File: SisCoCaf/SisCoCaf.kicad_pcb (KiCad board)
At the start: 2 copper layers, 20 parts, among them IC1 LPC111X_102, J1 Conn_01x02_Female, J2 Conn_01x02_Female, J3 Conn_01x03_Male, J4 Conn_01x03_Male, J5 Conn_01x01_Male, Q1 BC547, Q2 BC547, U1 LM317_TO39, U2 NRF24L01_Breakout

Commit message: Incorporar pila y jumper
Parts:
- moved IC1 37.5 mm to (135.0, 58.0)
- moved U2 26.9 mm to (109.0, 68.0), turned to 180 degrees
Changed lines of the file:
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@@
   )
   (module Package_DIP:DIP-28_W15.24mm_Socket (layer F.Cu)
-    (at 98 52)
+    (at 135 58)
     (descr "28-lead though-hole mounted DIP package, row spacing 15.24 mm (600 mils), Socket")
     (tags "THT DIP DIL PDIP 2.54mm 15.24mm 600mil Socket")
@@
   )
   (module RF_Module:nRF24L01_Breakout (layer F.Cu)
-    (at 129 50)
+    (at 109 68 180)
     (descr "nRF24L01 breakout board")
     (tags "nRF24L01 adapter breakout")
-    (fp_text reference U2 (at 0 -3) (layer F.SilkS)
-      (effects (font (size 1 1) (thickness 0.15)))
-    )
-    (fp_text value NRF24L01_Breakout (at 13 5) (layer F.Fab)
+    (fp_text reference U2 (at 0 -3 180) (layer F.SilkS)
+      (effects (font (size 1 1) (thickness 0.15)))
+    )
+    (fp_text value NRF24L01_Breakout (at 13 5 180) (layer F.Fab)
       (effects (font (size 1 1) (thickness 0.15)))
     )
@@
     (fp_line (start 27.75 13.5) (end 27.75 -2.25) (layer F.CrtYd) (width 0.05))
     (fp_line (start 27.75 -2.25) (end 27.75 -2.25) (layer F.CrtYd) (width 0.05))
-    (fp_text user %R (at 12.5 2.5) (layer F.Fab)
-      (effects (font (size 1 1) (thickness 0.15)))
-    )
-    (pad 1 thru_hole rect (at 0 0) (size 1.524 1.524) (drill 0.762) (layers *.Cu *.Mask)
-      (net 10 GND))
-    (pad 2 thru_hole circle (at 2.54 0) (size 1.524 1.524) (drill 0.762) (layers *.Cu *.Mask)
+    (fp_text user %R (at 12.5 2.5 180) (layer F.Fab)
+      (effects (font (size 1 1) (thickness 0.15)))
+    )
+    (pad 1 thru_hole rect (at 0 0 180) (size 1.524 1.524) (drill 0.762) (layers *.Cu *.Mask)
+      (net 10 GND))
+    (pad 2 thru_hole circle (at 2.54 0 180) (size 1.524 1.524) (drill 0.762) (layers *.Cu *.Mask)
       (net 8 VDD))
-    (pad 3 thru_hole circle (at 0 2.54) (size 1.524 1.524) (drill 0.762) (layers *.Cu *.Mask)
+    (pad 3 thru_hole circle (at 0 2.54 180) (size 1.524 1.524) (drill 0.762) (layers *.Cu *.Mask)
       (net 7 "Net-(IC1-Pad5)"))
-    (pad 4 thru_hole circle (at 2.54 2.54) (size 1.524 1.524) (drill 0.762) (layers *.Cu *.Mask)
+    (pad 4 thru_hole circle (at 2.54 2.54 180) (size 1.524 1.524) (drill 0.762) (layers *.Cu *.Mask)
       (net 14 "Net-(IC1-Pad4)"))
-    (pad 5 thru_hole circle (at 0 5.08) (size 1.524 1.524) (drill 0.762) (layers *.Cu *.Mask)
+    (pad 5 thru_hole circle (at 0 5.08 180) (size 1.524 1.524) (drill 0.762) (layers *.Cu *.Mask)
       (net 15 "Net-(IC1-Pad6)"))
-    (pad 6 thru_hole circle (at 2.54 5.08) (size 1.524 1.524) (drill 0.762) (layers *.Cu *.Mask)
+    (pad 6 thru_hole circle (at 2.54 5.08 180) (size 1.524 1.524) (drill 0.762) (layers *.Cu *.Mask)
       (net 16 "Net-(IC1-Pad2)"))
-    (pad 7 thru_hole circle (at 0 7.62) (size 1.524 1.524) (drill 0.762) (layers *.Cu *.Mask)
+    (pad 7 thru_hole circle (at 0 7.62 180) (size 1.524 1.524) (drill 0.762) (layers *.Cu *.Mask)
       (net 17 "Net-(IC1-Pad1)"))
-    (pad 8 thru_hole circle (at 2.54 7.62) (size 1.524 1.524) (drill 0.762) (layers *.Cu *.Mask)
+    (pad 8 thru_hole circle (at 2.54 7.62 180) (size 1.524 1.524) (drill 0.762) (layers *.Cu *.Mask)
       (net 18 "Net-(U2-Pad8)"))
     (model ${KISYS3DMOD}/RF_Module.3dshapes/nRF24L01_Breakout.wrl

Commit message: Modificando simbolos
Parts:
- removed J3: Conn_01x03_Male, Connector_PinHeader_1.00mm:PinHeader_1x03_P1.00mm_Vertical
- added BT1: Battery_Cell, Battery:BatteryHolder_Keystone_103_1x20mm, F.Cu at (99.0, 90.0)
- added J6: Conn_01x03_Male, Connector_JST:JST_XH_B03B-XH-A_1x03_P2.50mm_Vertical, F.Cu at (187.0, 94.0)
- added J7: Conn_01x02_Male, Connector_JST:JST_XH_B02B-XH-A_1x02_P2.50mm_Vertical, F.Cu at (187.0, 112.0)
- added JP1: Jumper, Connector_PinHeader_2.54mm:PinHeader_1x02_P2.54mm_Vertical, F.Cu at (96.0, 80.0)
- added MH1: MountingHole, MountingHole:MountingHole_2.2mm_M2, F.Cu at (106.0, 118.0)
- added MH2: MountingHole, MountingHole:MountingHole_2.2mm_M2, F.Cu at (168.0, 80.0)
- added MH3: MountingHole, MountingHole:MountingHole_2.2mm_M2, F.Cu at (166.0, 122.0)
- added MH4: MountingHole, MountingHole:MountingHole_2.2mm_M2, F.Cu at (103.0, 81.0)
- added R10: 220, Resistor_THT:R_Axial_DIN0204_L3.6mm_D1.6mm_P7.62mm_Horizontal, F.Cu at (143.0, 102.0)
- added R9: 220, Resistor_THT:R_Axial_DIN0204_L3.6mm_D1.6mm_P7.62mm_Horizontal, F.Cu at (180.0, 114.0)
- J1: value Conn_01x02_Female -> Entrada; footprint Connector_PinSocket_1.27mm:PinSocket_1x02_P1.27mm_Vertical -> Connector_JST:JST_XH_B02B-XH-A_1x02_P2.50mm_Vertical
- J2: footprint Connector_PinSocket_1.27mm:PinSocket_1x02_P1.27mm_Vertical -> Connector_PinSocket_2.54mm:PinSocket_1x02_P2.54mm_Vertical
- J4: value Conn_01x03_Male -> Conn_01x01_Male; footprint Connector_PinHeader_1.00mm:PinHeader_1x03_P1.00mm_Vertical -> Connector_PinHeader_2.54mm:PinHeader_1x01_P2.54mm_Vertical
- J5: value Conn_01x01_Male -> Conn_01x03_Male; footprint Connector_PinHeader_1.00mm:PinHeader_1x02_P1.00mm_Vertical -> Connector_JST:JST_XH_B03B-XH-A_1x03_P2.50mm_Vertical
- Q1, Q2: footprint Package_TO_SOT_THT:TO-92_Inline -> Package_TO_SOT_THT:TO-92_HandSolder
- R6, R7: value 220 -> 4k7
- U1: footprint Package_TO_SOT_THT:TO-39-3 -> Package_TO_SOT_THT:TO-220-3_Vertical
- moved J4 143.0 mm to (187.0, 105.0)
- moved J2 130.5 mm to (187.0, 123.0), turned to 180 degrees
- moved R5 115.4 mm to (173.0, 102.0), turned to 90 degrees
- moved D1 88.1 mm to (143.0, 113.0), turned to 270 degrees
- moved BZ1 84.1 mm to (126.0, 114.0)
- moved R1 69.3 mm to (120.0, 118.0), turned to 90 degrees
- moved R3 53.2 mm to (112.0, 105.0)
- moved J5 53.0 mm to (187.0, 82.0), turned to 270 degrees
- moved Q1 43.2 mm to (139.0, 110.0), turned to 90 degrees
- moved U2 42.5 mm to (141.0, 96.0)
- moved R8 42.4 mm to (180.0, 109.0), turned to 180 degrees
- moved J1 38.9 mm to (98.0, 122.0), turned to 90 degrees
- moved IC1 30.5 mm to (151.0, 84.0)
- moved R2 24.2 mm to (112.0, 118.0), turned to 90 degrees
- moved R6 21.2 mm to (173.0, 81.0), turned to 270 degrees
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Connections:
- net Net-(D1-Pad2) renamed /LED
- net Net-(IC1-Pad18) renamed /EntradaD1
- net Net-(IC1-Pad28) renamed /BUZZER
- IC1 pad 15: Net-(IC1-Pad15) -> /RX
- IC1 pad 16: Net-(IC1-Pad16) -> /TX
- IC1 pad 17: Net-(IC1-Pad17) -> /EntradaD2
- IC1 pad 25: Net-(IC1-Pad25) -> /SalidaD1
- IC1 pad 26: Net-(IC1-Pad26) -> /Sensor2
- IC1 pad 27: Net-(IC1-Pad27) -> /Sensor1
- J1 pad 1: Net-(J1-Pad1) -> GND
- J1 pad 2: Net-(J1-Pad2) -> +12V
- J2 pad 1: Net-(IC1-Pad16) -> /RX
- J2 pad 2: Net-(IC1-Pad15) -> /TX
- J4 pad 1: Net-(IC1-Pad27) -> Net-(J4-Pad1)
- J5 pad 1: Net-(J5-Pad1) -> VDD
- J5 pad 2: (no net) -> /Sensor1
- Q2 pad 1: Net-(J5-Pad1) -> Net-(J4-Pad1)
- R5 pad 1: Net-(J1-Pad2) -> Net-(Q2-Pad2)
- R5 pad 2: Net-(IC1-Pad17) -> /SalidaD1
- R6 pad 1: Net-(Q2-Pad2) -> /Sensor1
- R6 pad 2: Net-(IC1-Pad25) -> VDD
- R7 pad 1: Net-(D1-Pad1) -> /Sensor2
- R7 pad 2: GND -> VDD
- R8 pad 1: Net-(J1-Pad1) -> Net-(J7-Pad1)
- U1 pad 1: +12V -> Net-(R1-Pad2)
- U1 pad 2: Net-(R1-Pad2) -> VDD
- U1 pad 3: VDD -> +12V
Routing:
- net GND: track 0.00 -> 310.0 mm, vias 0 -> 6
- net VDD: track 0.00 -> 280.0 mm, vias 0 -> 4
- net /BUZZER: track 0.00 -> 52.7 mm
- net Net-(IC1-Pad5): track 0.00 -> 41.4 mm
- net Net-(IC1-Pad4): track 0.00 -> 39.8 mm
- net /Sensor1: track 0.00 -> 36.0 mm
- net Net-(R1-Pad2): track 0.00 -> 31.1 mm
- net /Sensor2: track 0.00 -> 23.9 mm
- net /RX: track 0.00 -> 23.2 mm
- net /TX: track 0.00 -> 23.0 mm
- net Net-(IC1-Pad2): track 0.00 -> 21.7 mm, vias 0 -> 2
- net Net-(Q1-Pad2): track 0.00 -> 19.6 mm
- net Net-(IC1-Pad6): track 0.00 -> 15.4 mm, vias 0 -> 2
- net Net-(BT1-Pad1): track 0.00 -> 13.4 mm
- net Net-(IC1-Pad1): track 0.00 -> 11.8 mm
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- added copper zone on B.Cu, net GND
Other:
- board outline added: 100 x 50 mm
- net class Default: clearance 0.2 -> 0.8; trace_width 0.25 -> 0.8
- rule trace_clearance: 0.2 -> 0.8
- rule trace_min: 0.2 -> 0.6
- board text added: "2018"
- board text added: "Grilla 1mm. Pista 0.8mm. Margen: 0,8mm. Vías: 0,8mm Agujeros: 2mm. Transferencia por técnica del planchado en una capa."
- board text added: "IND. ARG."
- board text added: "Sensor 1"
- board text added: "Sensor 2"
- board text added: "SisCoCaF 2018"

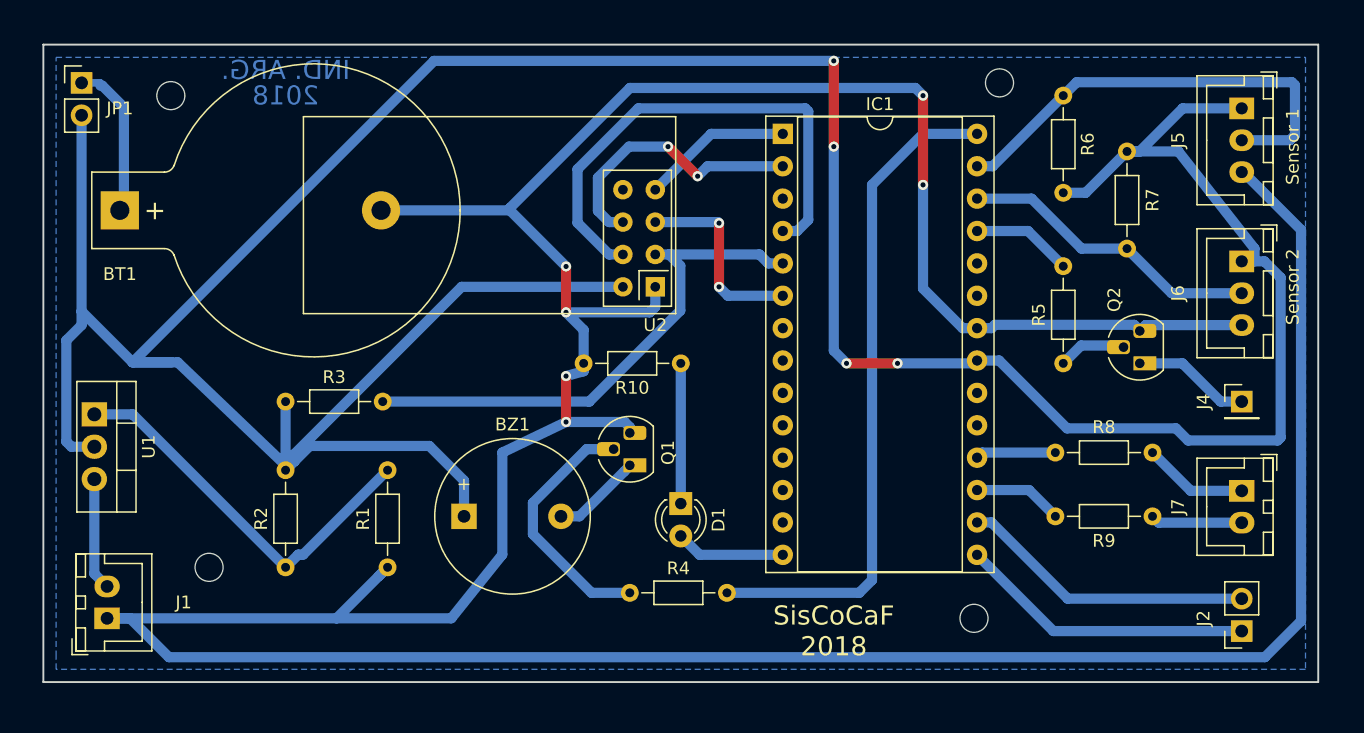
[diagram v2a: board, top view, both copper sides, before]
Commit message: Versión final.
Realizo correcciones indicadas por profesor.
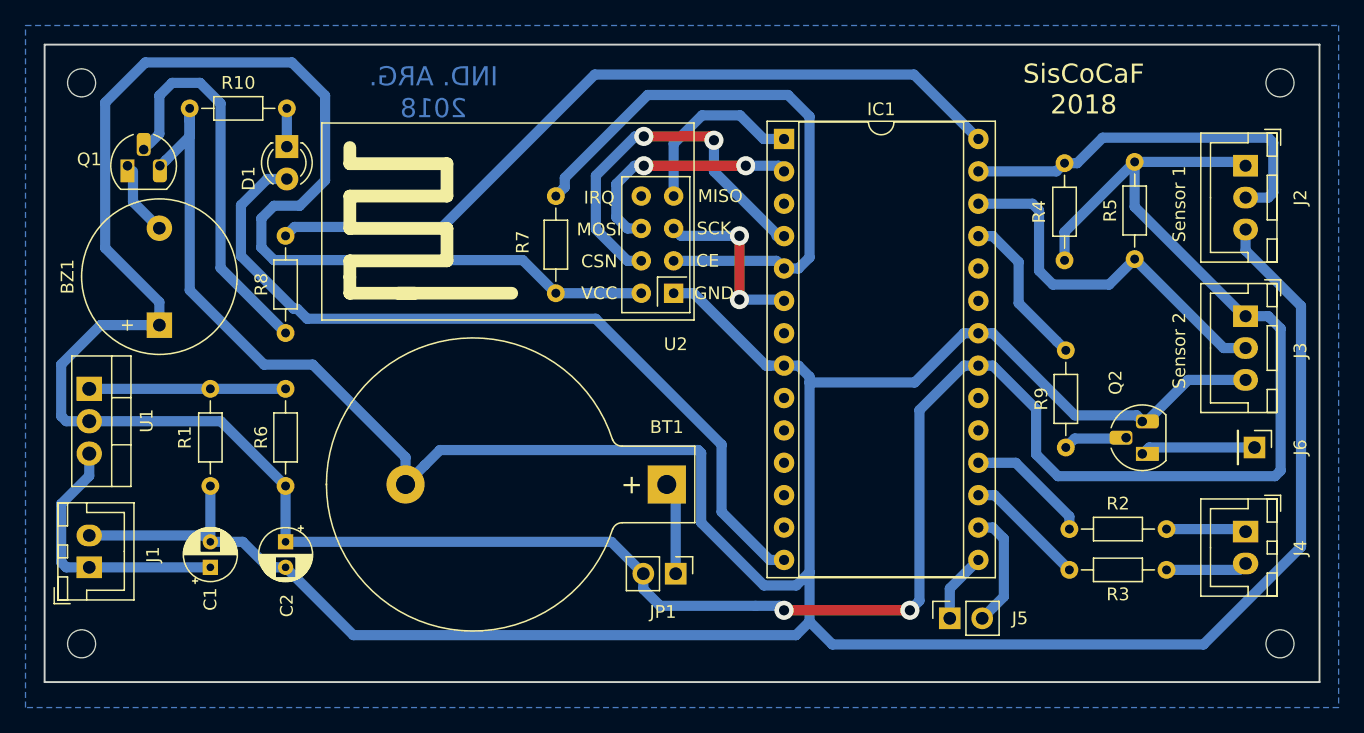
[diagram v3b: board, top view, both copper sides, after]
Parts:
- removed J7: Conn_01x02_Male, Connector_JST:JST_XH_B02B-XH-A_1x02_P2.50mm_Vertical
- added C1: 100uf, Capacitor_THT:CP_Radial_D4.0mm_P2.00mm, F.Cu at (106.1, 118.0)
- added C2: 220uf, Capacitor_THT:CP_Radial_D4.0mm_P2.00mm, F.Cu at (112.0, 116.0)
- added J3: Conn_01x03_Male, Connector_JST:JST_XH_B03B-XH-A_1x03_P2.50mm_Vertical, F.Cu at (187.3, 98.3)
- J2: value Conn_01x02_Female -> Conn_01x03_Male; footprint Connector_PinSocket_2.54mm:PinSocket_1x02_P2.54mm_Vertical -> Connector_JST:JST_XH_B03B-XH-A_1x03_P2.50mm_Vertical
- J4: value Conn_01x01_Male -> Conn_01x02_Male; footprint Connector_PinHeader_2.54mm:PinHeader_1x01_P2.54mm_Vertical -> Connector_JST:JST_XH_B02B-XH-A_1x02_P2.50mm_Vertical
- J5: value Conn_01x03_Male -> Conn_01x02_Female; footprint Connector_JST:JST_XH_B03B-XH-A_1x03_P2.50mm_Vertical -> Connector_PinSocket_2.54mm:PinSocket_1x02_P2.54mm_Vertical
- J6: value Conn_01x03_Male -> Conn_01x01_Male; footprint Connector_JST:JST_XH_B03B-XH-A_1x03_P2.50mm_Vertical -> Connector_PinHeader_2.54mm:PinHeader_1x01_P2.54mm_Vertical
- R2: value 1k -> 220
- R3: value 5k6 -> 220
- R4, R5: value 220 -> 4k7
- R6: value 4k7 -> 1k
- R7: value 4k7 -> 5k6
- U2: footprint RF_Module:nRF24L01_Breakout -> RF_Module:nRF24L01_Breakout_antena
- moved R3 70.3 mm to (181.1, 118.2), turned to 180 degrees
- moved R2 69.2 mm to (181.1, 115.0), turned to 180 degrees
- moved R8 68.6 mm to (112.0, 99.6), turned to 90 degrees
- moved R6 68.3 mm to (112.0, 111.6), turned to 90 degrees
- moved JP1 60.4 mm to (142.6, 118.5), turned to 270 degrees
- moved BT1 48.0 mm to (141.9, 111.5), turned to 180 degrees
- moved R4 47.9 mm to (173.1, 86.3), turned to 270 degrees
- moved J5 46.1 mm to (164.1, 122.0), turned to 90 degrees
- moved Q1 45.9 mm to (99.6, 86.5), turned to 0 degrees
- moved R7 44.9 mm to (133.2, 96.5)
- moved D1 41.7 mm to (112.1, 85.0)
- moved R10 36.8 mm to (112.1, 82.0)
- moved J2 36.5 mm to (187.3, 86.5), turned to 270 degrees
- moved BZ1 28.2 mm to (102.1, 99.0), turned to 90 degrees
- moved MH3 24.1 mm to (190.0, 124.0)
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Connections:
- IC1 pad 8: Net-(IC1-Pad8) -> GND
- J1 pad 1: GND -> +12V
- J1 pad 2: +12V -> GND
- J2 pad 1: /RX -> VDD
- J2 pad 2: /TX -> /Sensor1
- J5 pad 1: VDD -> /RX
- J5 pad 2: /Sensor1 -> /TX
- J6 pad 1: VDD -> Net-(J6-Pad1)
- Q2 pad 1: Net-(J4-Pad1) -> Net-(J6-Pad1)
- R1 pad 1: GND -> Net-(R1-Pad1)
- R1 pad 2: Net-(R1-Pad2) -> GND
- R2 pad 1: Net-(R1-Pad2) -> Net-(J4-Pad1)
- R2 pad 2: VDD -> /EntradaD1
- R3 pad 1: VDD -> Net-(J4-Pad2)
- R3 pad 2: Net-(IC1-Pad5) -> /EntradaD2
- R4 pad 1: Net-(Q1-Pad2) -> /Sensor1
- R4 pad 2: /BUZZER -> VDD
- R5 pad 1: Net-(Q2-Pad2) -> /Sensor2
- R5 pad 2: /SalidaD1 -> VDD
- R6 pad 1: /Sensor1 -> VDD
- R6 pad 2: VDD -> Net-(R1-Pad1)
- R7 pad 1: /Sensor2 -> VDD
- R7 pad 2: VDD -> Net-(IC1-Pad5)
- R8 pad 1: Net-(J7-Pad1) -> Net-(Q1-Pad2)
- R8 pad 2: /EntradaD1 -> /BUZZER
- R9 pad 1: Net-(J7-Pad2) -> Net-(Q2-Pad2)
- R9 pad 2: /EntradaD2 -> /SalidaD1
- U1 pad 1: Net-(R1-Pad2) -> Net-(R1-Pad1)
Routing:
- net /LED: track 8.61 -> 64.0 mm
- net Net-(R1-Pad2): track 31.1 -> 0.00 mm
- net GND: track 310.0 -> 292.0 mm, vias 6 -> 0
- net /RX: track 23.2 -> 5.51 mm
- net Net-(R1-Pad1): track 0.00 -> 15.4 mm
- net /TX: track 23.0 -> 9.32 mm
- net +12V: track 8.83 -> 20.9 mm
- net Net-(Q1-Pad2): track 19.6 -> 30.1 mm
- net Net-(IC1-Pad4): track 39.8 -> 30.1 mm, vias 0 -> 2
- net Net-(J6-Pad1): track 0.00 -> 8.99 mm
- net /BUZZER: track 52.7 -> 61.7 mm
- net Net-(J7-Pad1): track 8.24 -> 0.00 mm
- net Net-(D1-Pad1): track 11.0 -> 3.00 mm
- net Net-(J7-Pad2): track 7.21 -> 0.00 mm
- net Net-(J4-Pad2): track 0.00 -> 6.41 mm
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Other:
- net class Default: via_dia 0.8 -> 1.5; via_drill 0.4 -> 0.8
- rule via_min_drill: 0.3 -> 0.8
- rule via_min_size: 0.4 -> 1.5
- board text added: "Grilla: 1 mm. Pista: 0.8 mm. Margen: 0,8 mm. Vías: 0,8 mm Agujeros fijación: 2,2 mm Transferencia por técnica del planchado en una capa."
- board text removed: "Grilla 1mm. Pista 0.8mm. Margen: 0,8mm. Vías: 0,8mm Agujeros: 2mm. Transferencia por técnica del planchado en una capa."
